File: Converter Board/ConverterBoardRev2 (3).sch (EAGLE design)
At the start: 28 parts

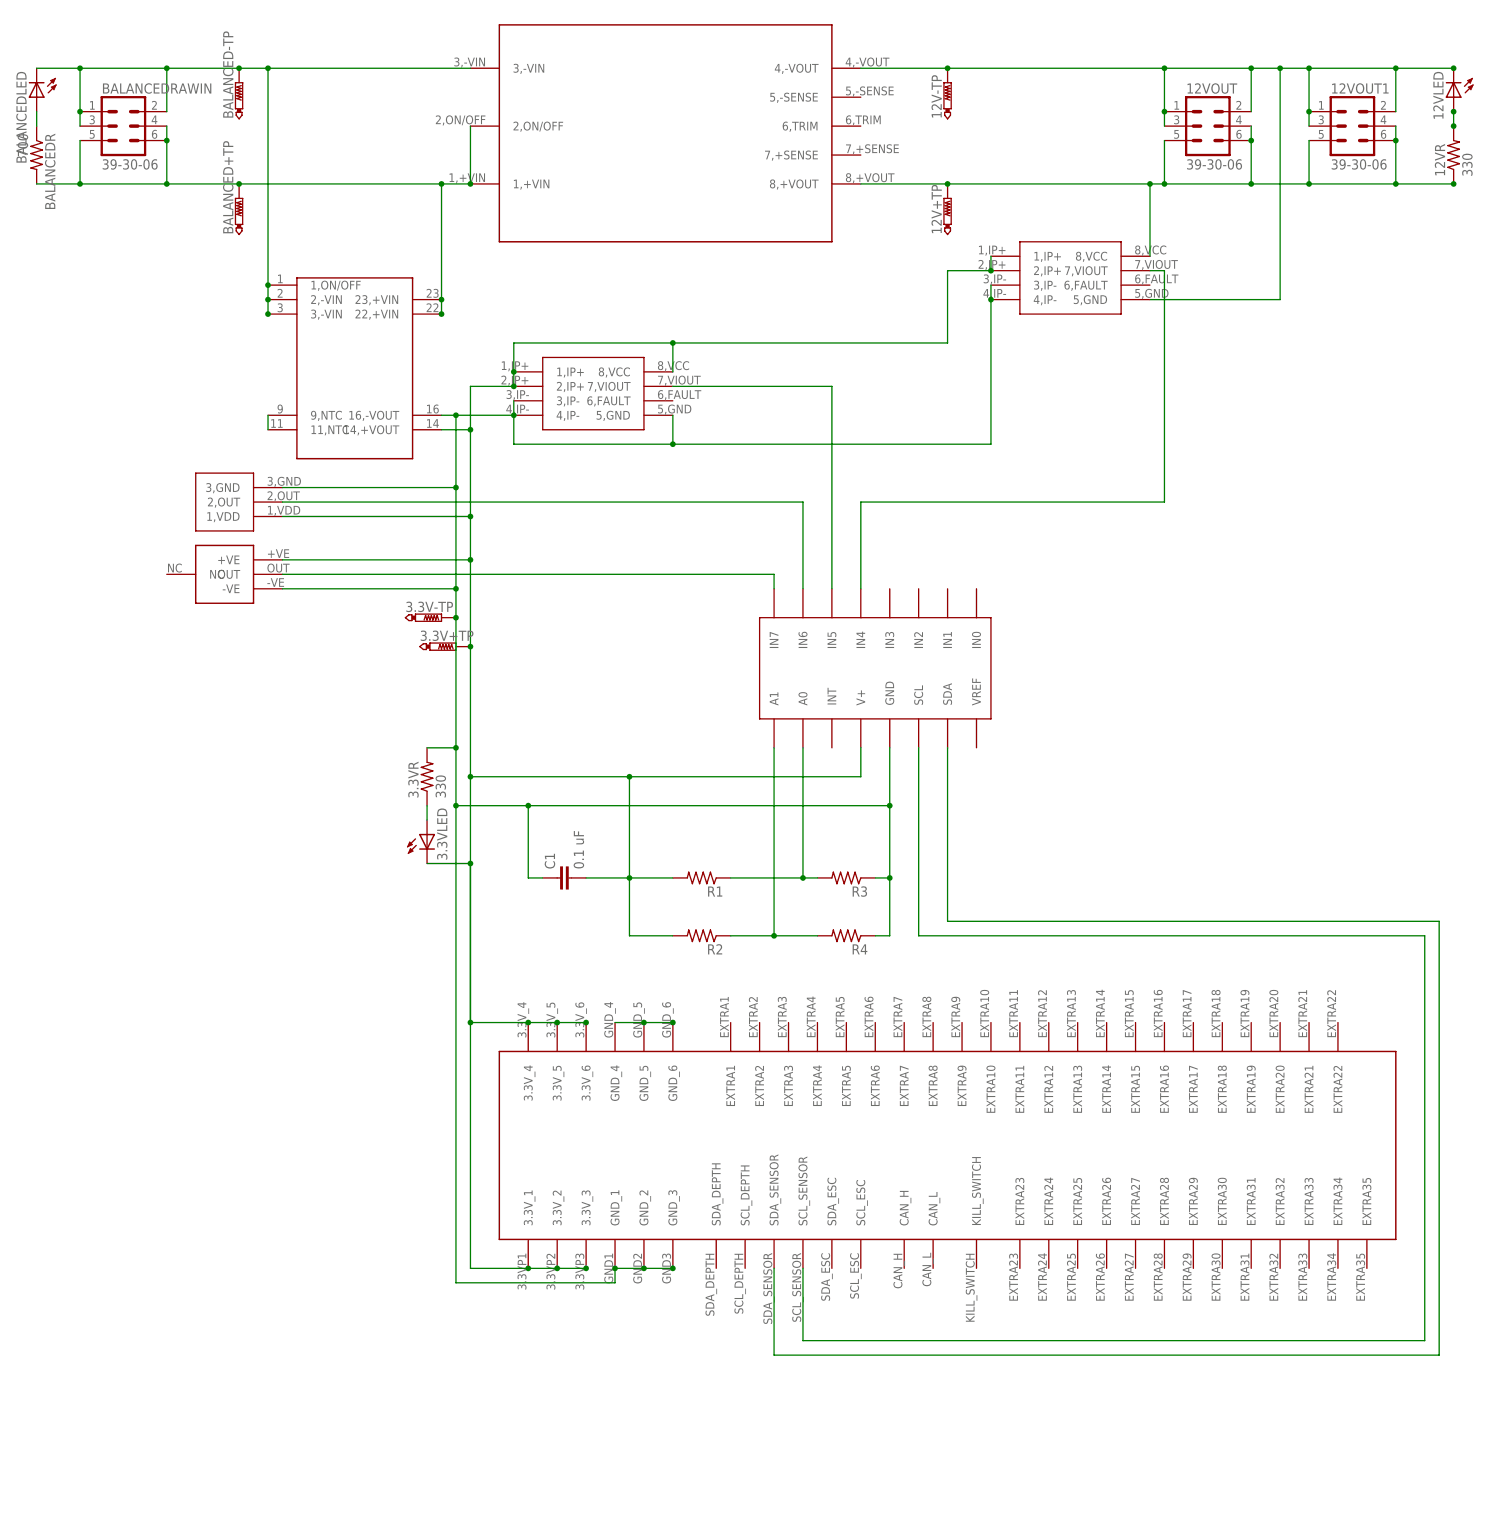
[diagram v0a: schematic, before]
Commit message: Computer might blow up
Schematic done
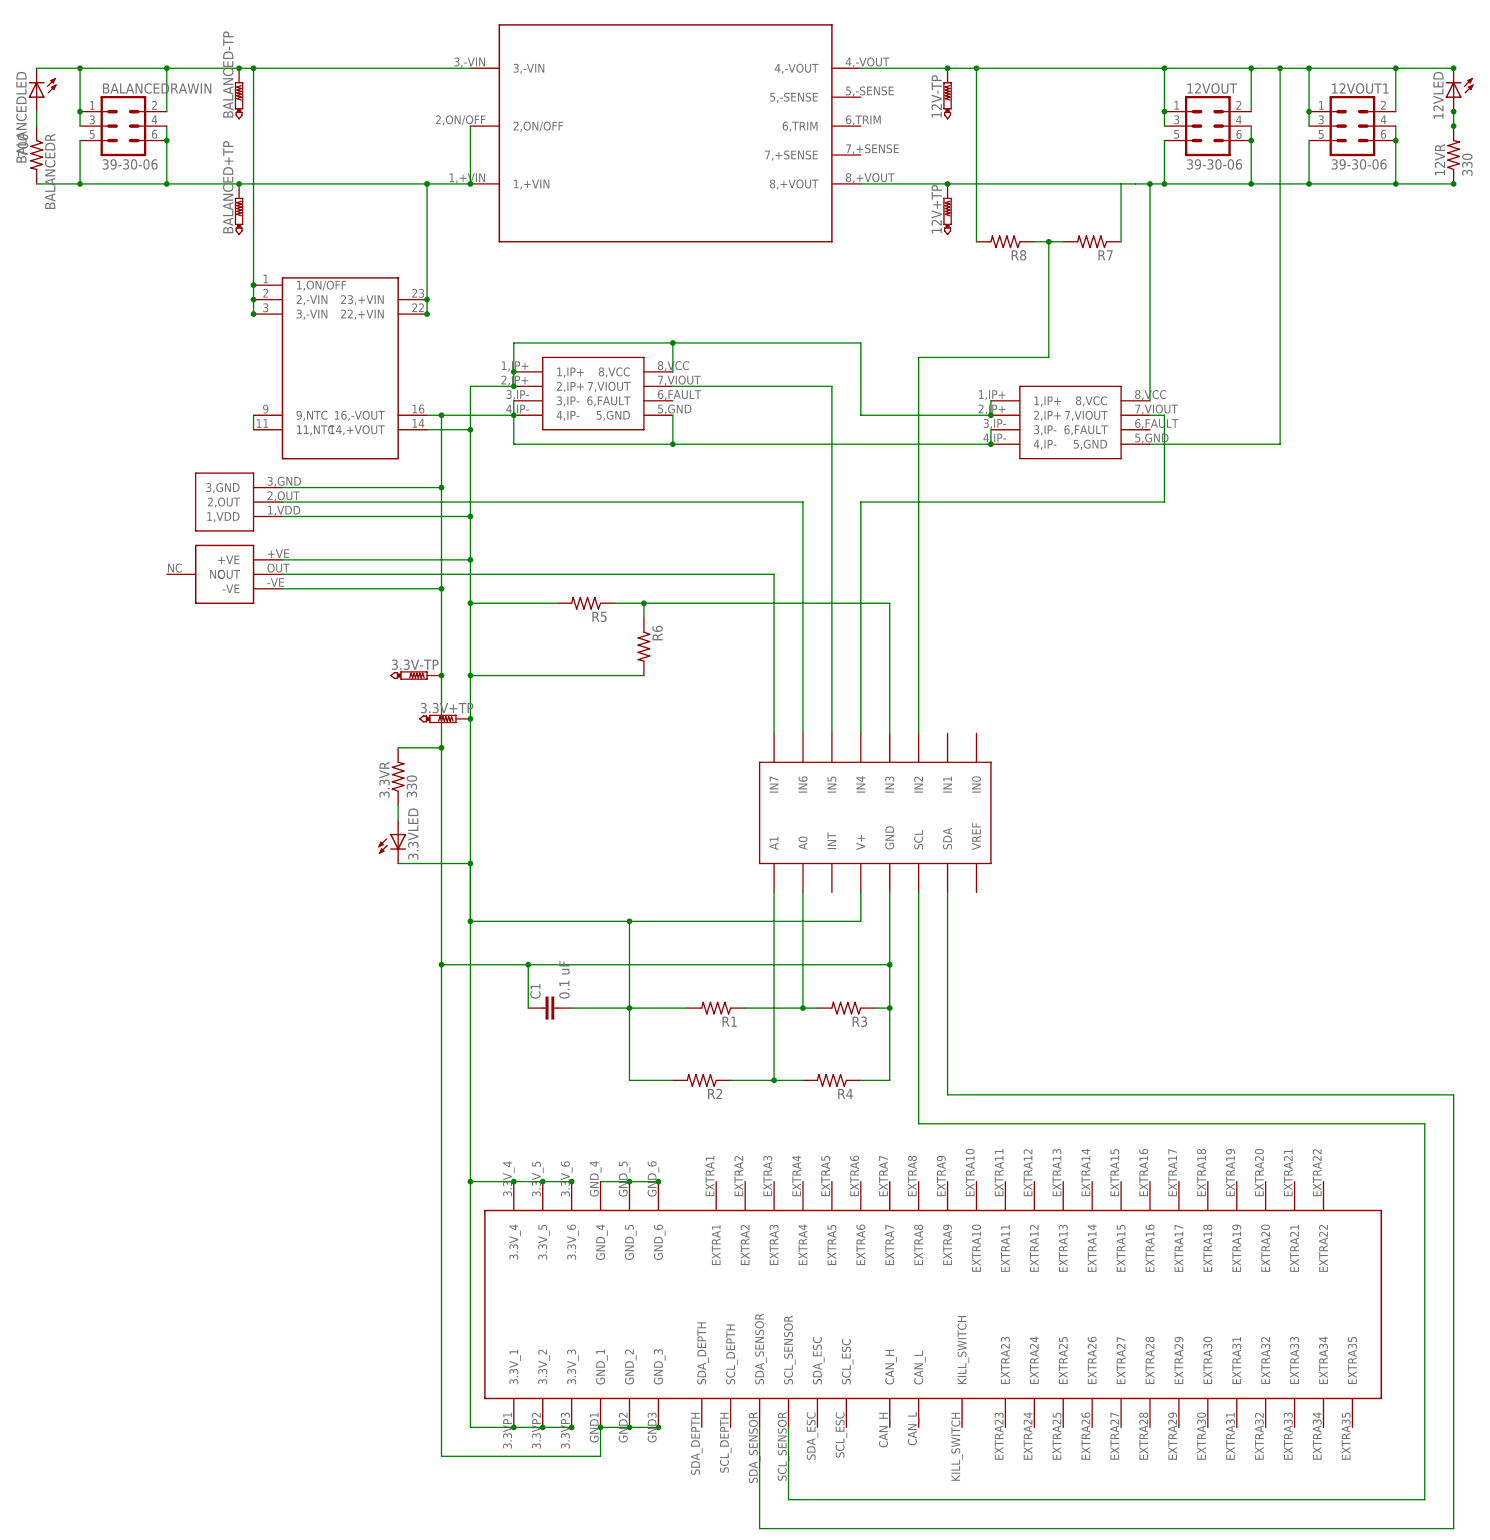
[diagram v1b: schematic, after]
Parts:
- added R5, R6, R7, R8: (no value), resistor:R-US_0204/7
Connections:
- net N$2 renamed 3.3IDATA
- net N$3 renamed 12IDATA
- net N$5 renamed A0
- net N$6 renamed A1
- net N$7 renamed SCL
- net N$8 renamed SDA
- new net 12VDATA: R7.2, R8.1, U$8.IN2
- new net 3.3VDATA: R5.1, R6.1, U$8.IN3
- net 12V+: now also R7.1
- net 12V-: now also R8.2
- net 3.3V+: now also R5.2, R6.2
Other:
- moved on the sheet: 3.3V+TP, 3.3V-TP, 3.3VLED, 3.3VR, C1, R1, R2, R3, R4
